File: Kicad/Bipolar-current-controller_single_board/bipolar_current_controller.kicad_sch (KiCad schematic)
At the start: 92 parts, among them J1 Error signal, J2 Set point, J4 Monitor, J5 Conn_02x04_Counter_Clockwise, J6 Enable, J7 P-MOS, J8 N-MOS, J9 Shunt resistor, U1 AD8421, U19 FOD8482TR2, U2 AD8421, U3 AD8421, U4 OPA388, U5 LT1363, U6 LT1363, U7 BUF634A, U8 BUF634A

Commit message: Corrections of the design after modification of package
1) The switches were short circuited, I had to remove offending via connections from under the packages.
2) F.Fab larer has been cleaned up a bit: this will allow for printing a mounting diagram.
3) In the schematic the GND label has been substituted with teh GND symbol.
4) Added comments about J5 connector.
5) Removed .~lock.BOM.csv# that was committed by mistake
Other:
- note added: "J5 is used to host the feedback network tuned for the inductor. pins 1-8 are for the high frequency capacitor pind 3-6 and 2-7 are for the integrating capaciror and the proportional gain"

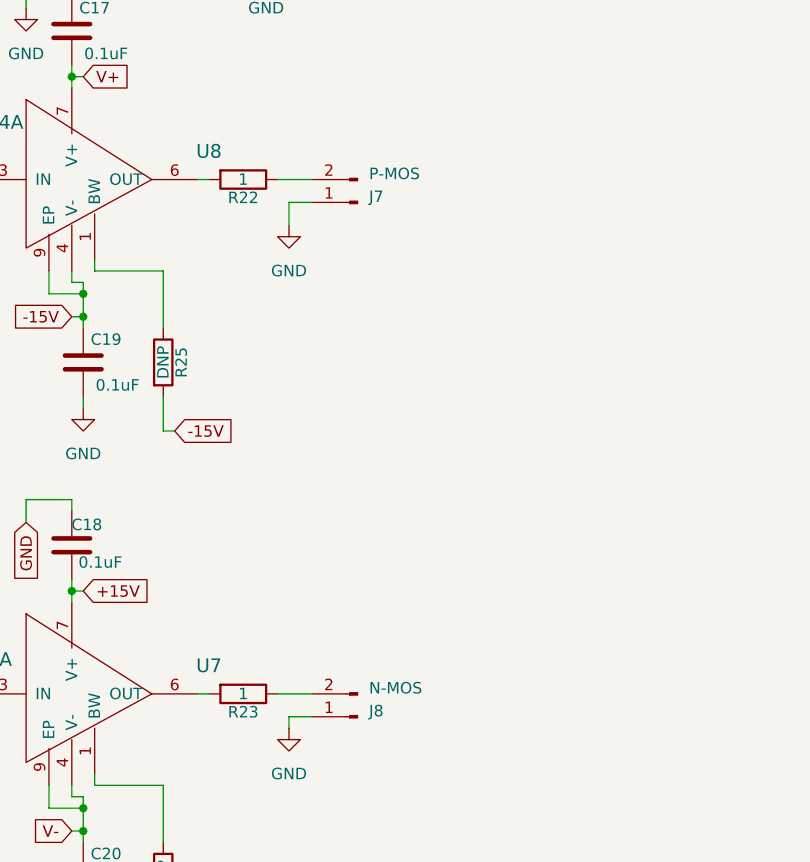
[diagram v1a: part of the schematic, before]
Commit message: Swap P-MOS and N-MOS labels
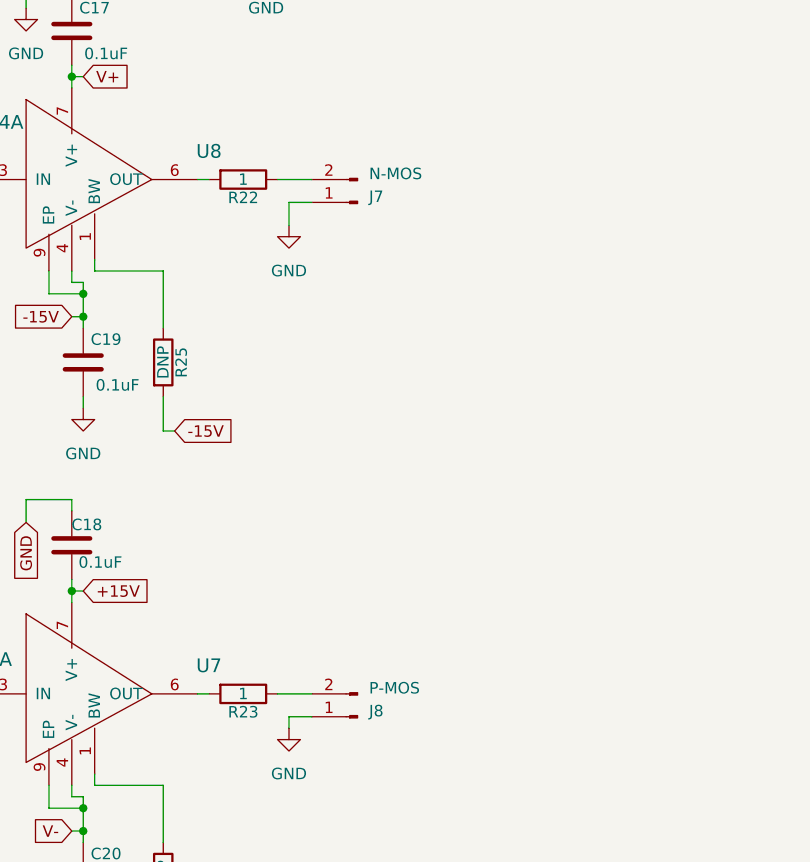
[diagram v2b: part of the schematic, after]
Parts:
- J7: value P-MOS -> N-MOS
- J8: value N-MOS -> P-MOS
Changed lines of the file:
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@@
       (effects (font (size 1.27 1.27)) (justify right))
     )
-    (property "Value" "P-MOS" (at 297.18 106.045 0)
+    (property "Value" "N-MOS" (at 297.18 106.045 0)
       (effects (font (size 1.27 1.27)) (justify right))
     )
@@
       (effects (font (size 1.27 1.27)) (justify right))
     )
-    (property "Value" "N-MOS" (at 297.18 163.195 0)
+    (property "Value" "P-MOS" (at 297.18 163.195 0)
       (effects (font (size 1.27 1.27)) (justify right))
     )
